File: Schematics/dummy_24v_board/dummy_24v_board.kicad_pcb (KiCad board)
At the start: 2 copper layers, 69.5 x 60 mm, 1 part, among them J1 Stack Male Edge Connector

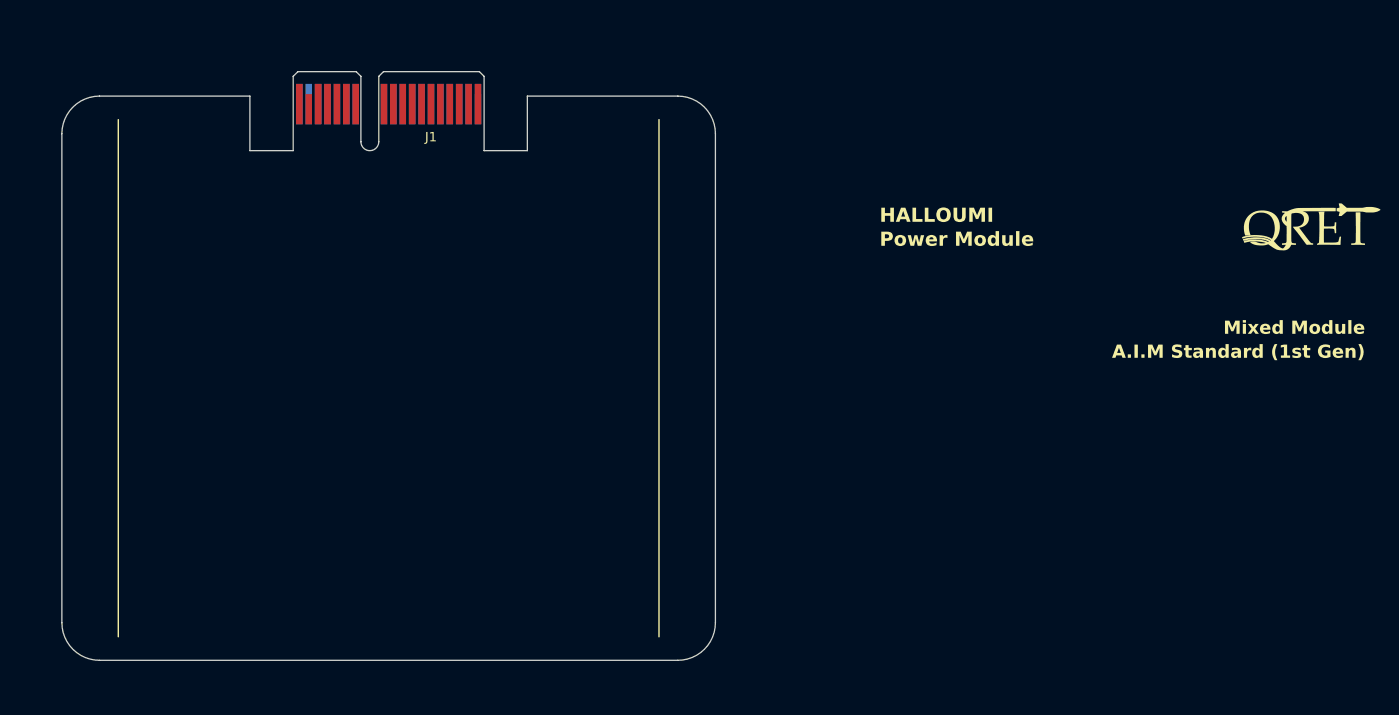
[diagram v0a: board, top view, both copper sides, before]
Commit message: added 3.3V,5V,CAN
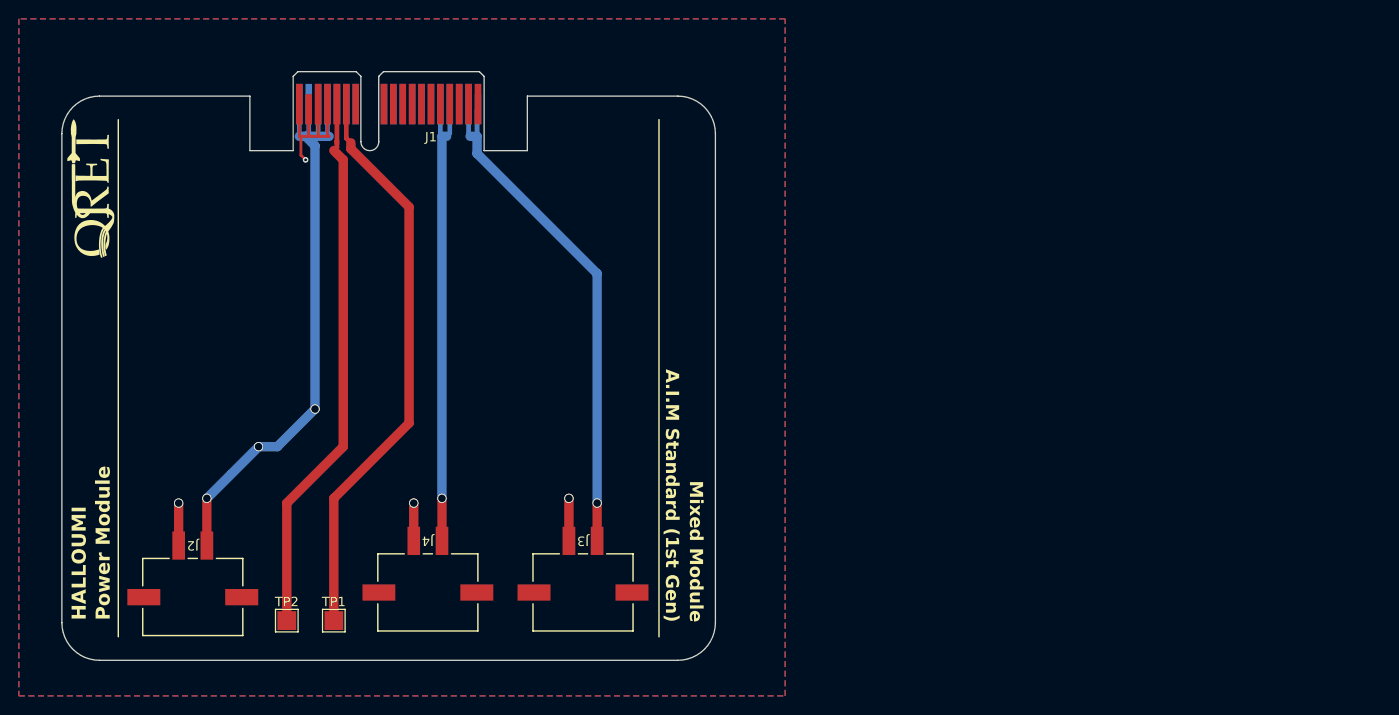
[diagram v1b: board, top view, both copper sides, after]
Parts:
- added J2: Conn_01x02_Socket, footprints:CONN_2-1445057-2_TYCO, F.Cu at (38.0, 69.5)
- added J3: Conn_01x02_Socket, footprints:CONN_2-1445057-2_TYCO, F.Cu at (79.5, 69.0)
- added J4: Conn_01x02_Socket, footprints:CONN_2-1445057-2_TYCO, F.Cu at (63.0, 69.0)
- added TP1: TestPoint, TestPoint:TestPoint_Pad_2.0x2.0mm, F.Cu at (51.5, 77.5)
- added TP2: TestPoint, TestPoint:TestPoint_Pad_2.0x2.0mm, F.Cu at (46.5, 77.5)
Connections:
- net 5.0V_A renamed +5V
- net Net-(J1-24V_C-PadA15) renamed +24V
- net Net-(J1-3.3V_A-PadA1) renamed +3.3V
- net Net-(J1-GND_C-PadB15) renamed GND
- J1 pad B13: unconnected-(J1-CAN_L-PadB13) -> CAN_L
- J1 pad B14: unconnected-(J1-CAN_H-PadB14) -> CAN_H
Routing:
- net +24V: track 0.00 -> 66.8 mm, vias 0 -> 3
- net CAN_L: track 0.00 -> 61.0 mm
- net CAN_H: track 0.00 -> 58.3 mm
- net +3.3V: track 0.00 -> 55.4 mm, vias 0 -> 1
- net +5V: track 0.00 -> 50.6 mm, vias 0 -> 1
- net GND: track 0.00 -> 32.3 mm, vias 0 -> 4
- added copper zone on B.Cu, net GND
- added copper zone on F.Cu, net GND

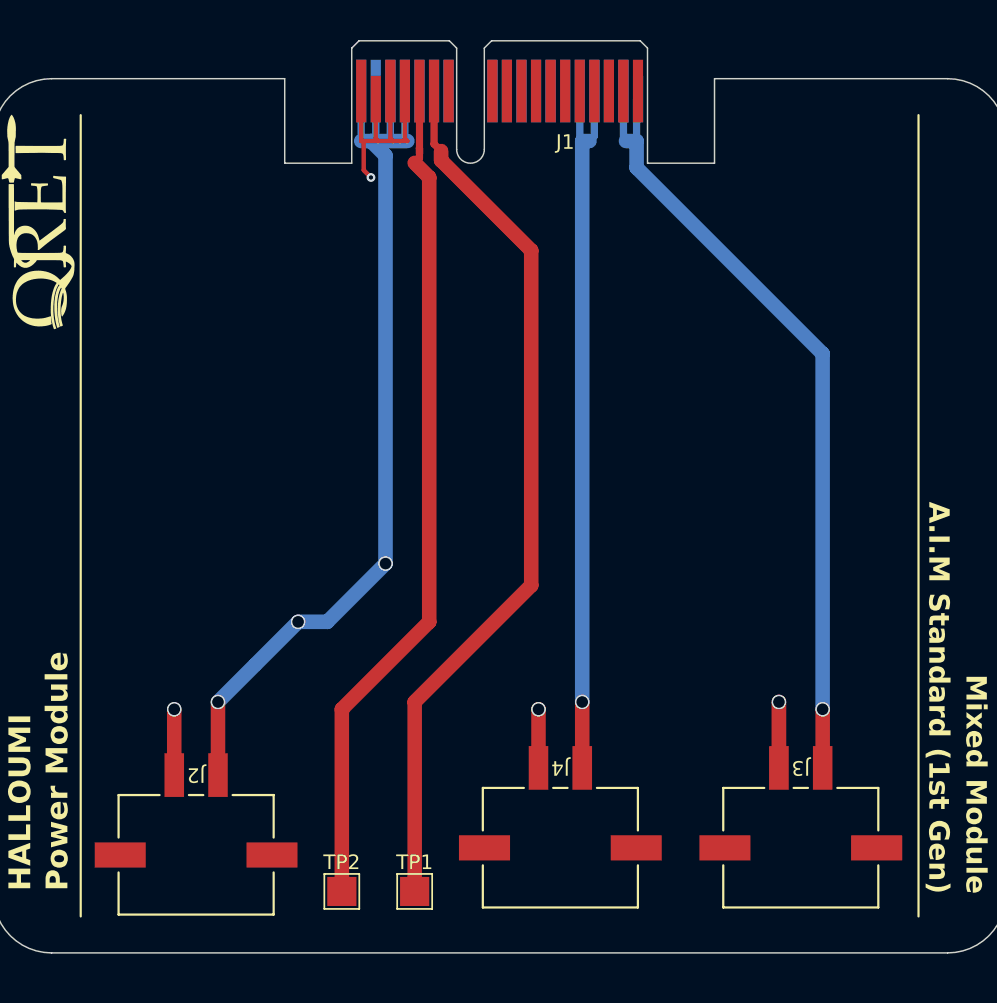
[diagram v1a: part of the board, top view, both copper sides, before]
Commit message: added two TestPoints for BATT 1&2
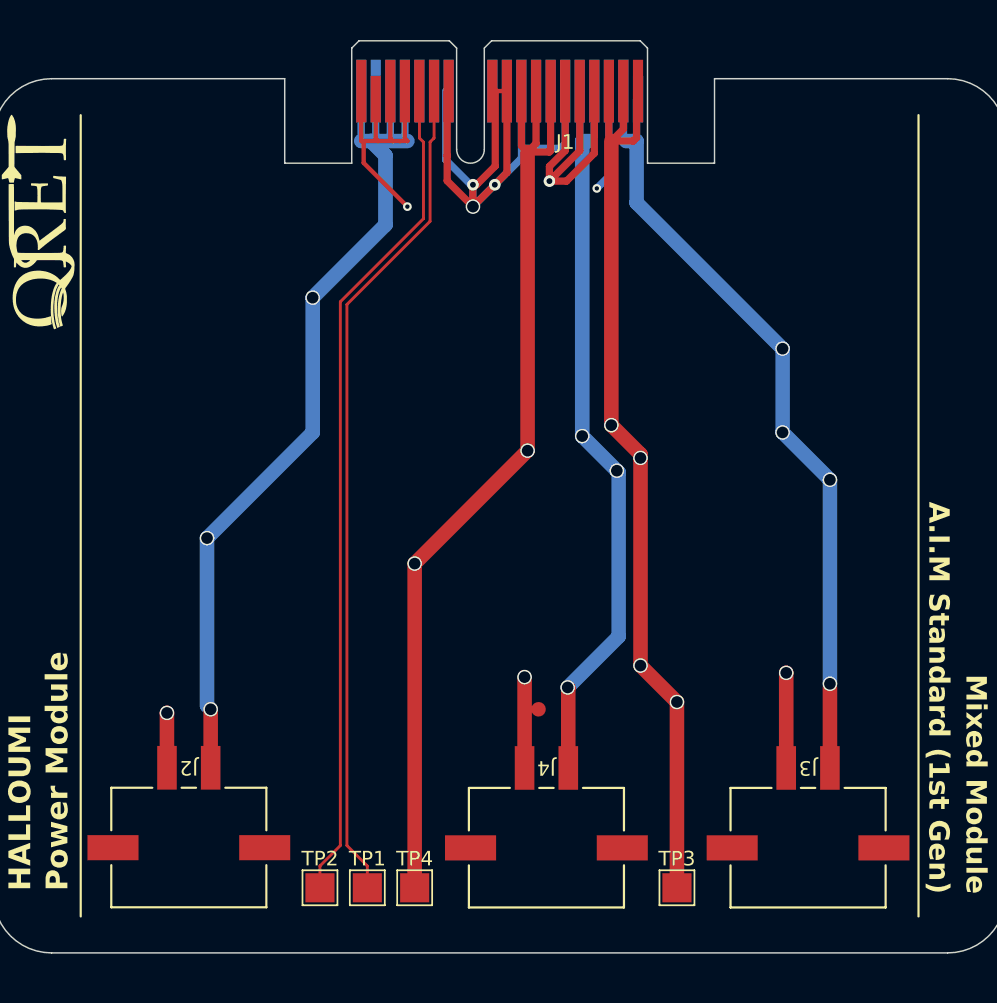
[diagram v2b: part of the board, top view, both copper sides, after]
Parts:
- added TP3: TestPoint, TestPoint:TestPoint_Pad_2.0x2.0mm, F.Cu at (69.5, 77.2)
- added TP4: TestPoint, TestPoint:TestPoint_Pad_2.0x2.0mm, F.Cu at (51.5, 77.2)
- moved TP1 3.26 mm to (48.2, 77.2)
- moved TP2 1.52 mm to (45.0, 77.2)
- moved J4 0.96 mm to (62.0, 69.0)
- moved J2 0.71 mm to (37.5, 69.0)
- moved J3 0.50 mm to (80.0, 69.0)
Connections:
- net CAN_H renamed CAN_+
- net CAN_L renamed CAN_-
- net Net-(J1-BATT_A-PadB1) renamed /BATT_1
- net Net-(J1-BATT_B-PadB7) renamed /BATT_2
- J1 pad A12: Net-(J1-GND_B-PadA12) -> GND
- J1 pad A3: Net-(J1-GND_A-PadA3) -> GND
- J1 pad A6: Net-(J1-GND_A-PadA3) -> GND
- J1 pad A7: Net-(J1-3.3V_B-PadA7) -> +3.3V
- J1 pad A8: Net-(J1-3.3V_B-PadA7) -> +3.3V
- J1 pad A9: Net-(J1-GND_B-PadA12) -> GND
- J1 pad B10: Net-(J1-GND_B-PadA12) -> GND
- J1 pad B11: Net-(J1-GND_B-PadA12) -> GND
- J1 pad B12: Net-(J1-GND_B-PadA12) -> GND
- J1 pad B4: Net-(J1-GND_A-PadA3) -> GND
- J1 pad B5: Net-(J1-GND_A-PadA3) -> GND
- J1 pad B6: Net-(J1-GND_A-PadA3) -> GND
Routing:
- net GND: track 32.3 -> 119.9 mm, vias 4 -> 9
- net /BATT_2: track 0.00 -> 68.2 mm, vias 0 -> 2
- net /BATT_1: track 0.00 -> 65.4 mm, vias 0 -> 4
- net CAN_-: track 61.0 -> 57.7 mm
- net +5V: track 50.6 -> 53.1 mm, vias 1 -> 3
- net +24V: track 66.8 -> 65.7 mm
- net CAN_+: track 58.3 -> 57.7 mm
- net +3.3V: track 55.4 -> 55.1 mm, vias 1 -> 4

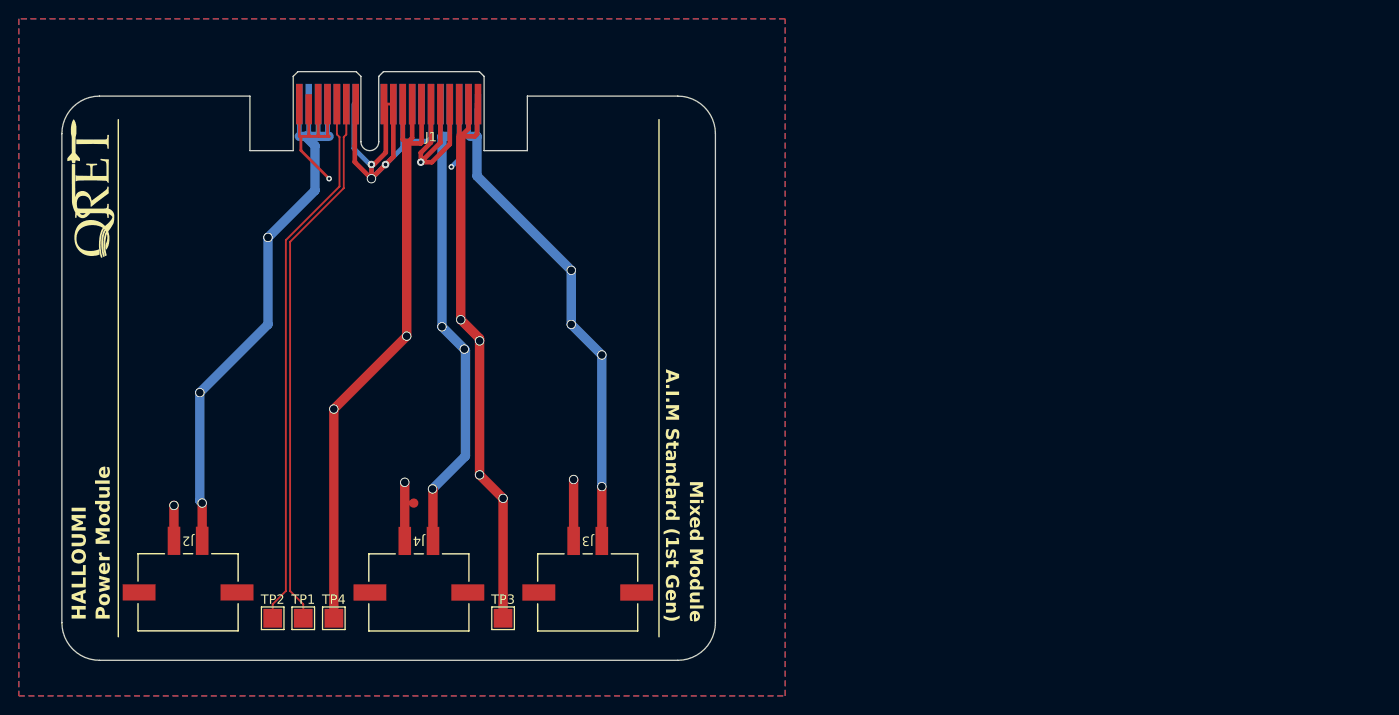
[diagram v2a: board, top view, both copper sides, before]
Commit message: gnd vias added
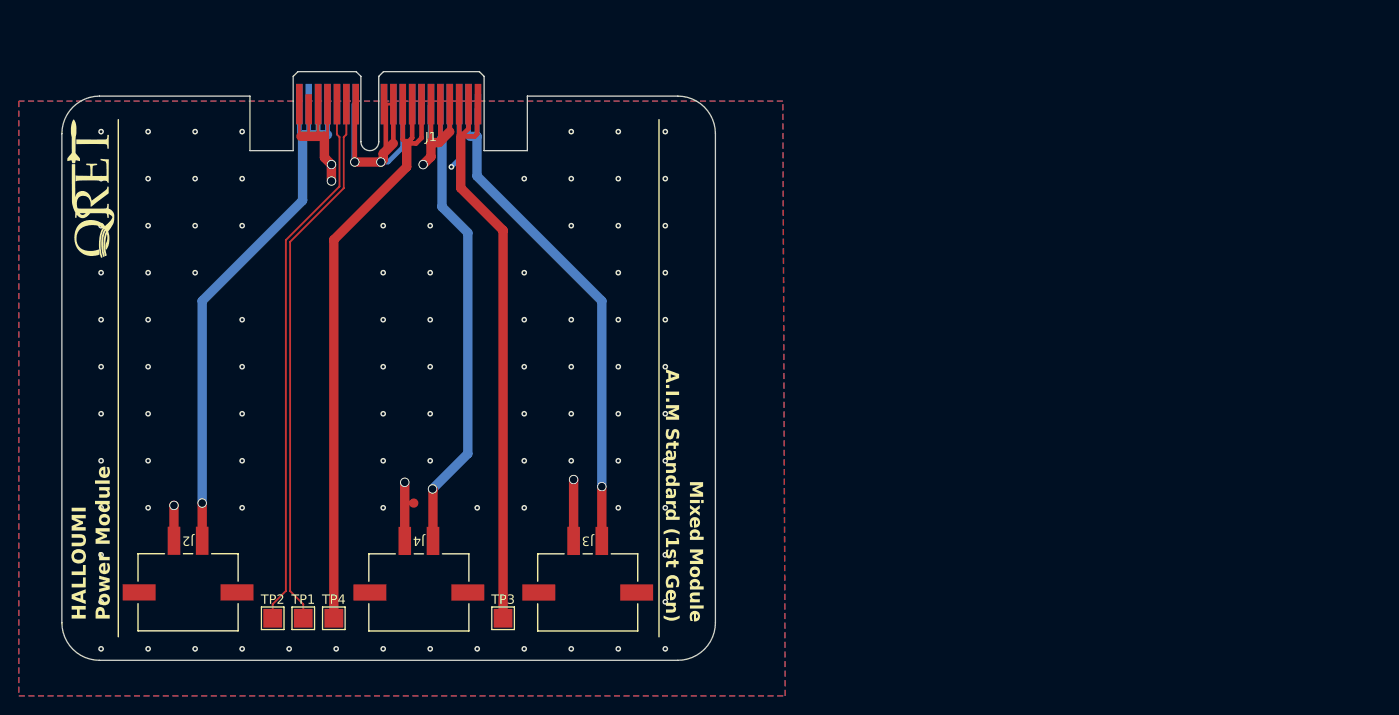
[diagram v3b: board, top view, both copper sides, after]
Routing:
- net GND: track 119.9 -> 104.0 mm, vias 9 -> 102
- net +24V: track 65.7 -> 63.4 mm, vias 3 -> 1
- net /BATT_2: track 68.2 -> 67.9 mm, vias 2 -> 0
- net +5V: track 53.1 -> 53.2 mm, vias 3 -> 1
- net /BATT_1: vias 4 -> 0
- net +3.3V: vias 4 -> 1
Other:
- board text removed: "USE GRID THAT IS SOME MULTIPLE OF 0.1mm (0.1mm, 0.2mm, 0.5mm, 1.0mm, etc)"

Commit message: Vias modified
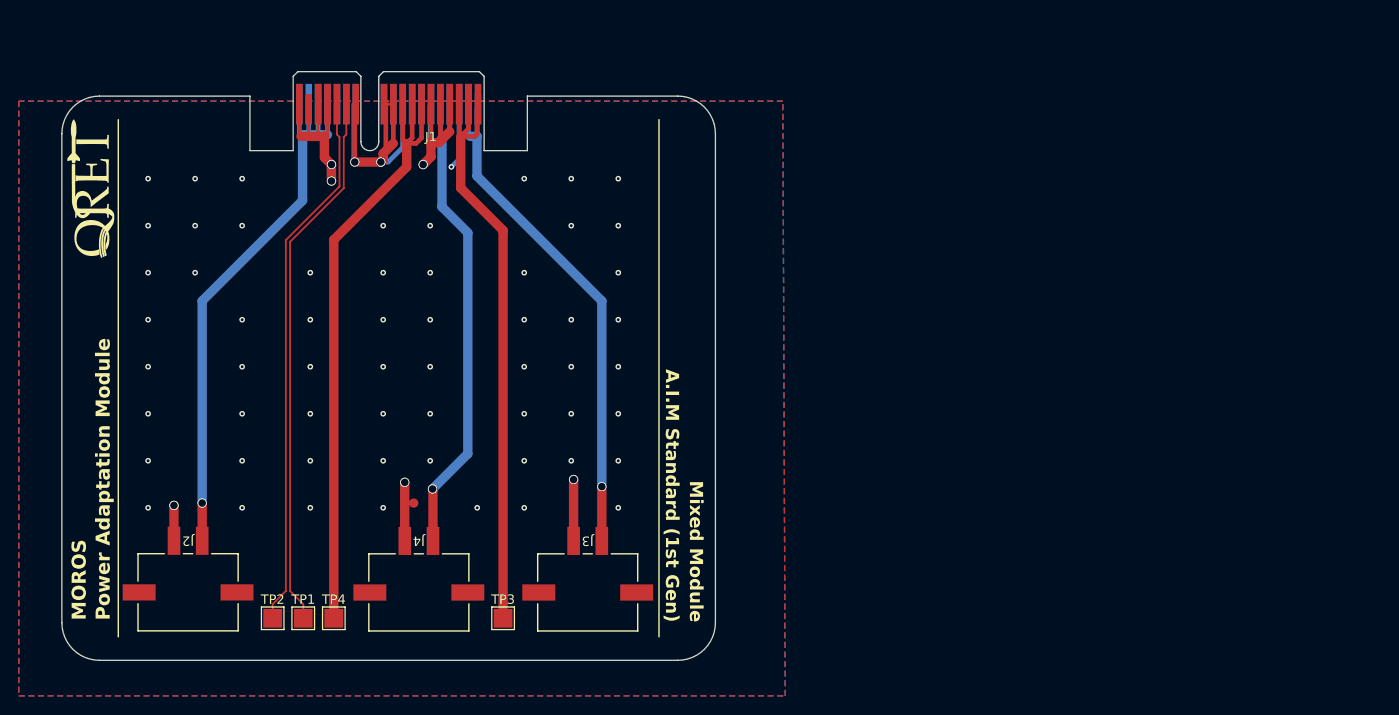
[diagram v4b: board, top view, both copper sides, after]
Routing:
- net GND: vias 102 -> 68
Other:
- board text added: "MOROS"
- board text added: "Moros V1.0 QRET Feb 2026 Johann Samuel Nana"
- board text added: "Power Adaptation Module"
- board text removed: "HALLOUMI"
- board text removed: "Power Module"

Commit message: Connectors model added
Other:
- board text added: "A.I.M Standard (2nd Gen)"
- board text added: "MORROS"
- board text added: "Morros V1.0 QRET Feb 2026 Johann Samuel Nana"
- board text removed: "A.I.M Standard (1st Gen)"
- board text removed: "MOROS"
- board text removed: "Mixed Module"
- board text removed: "Moros V1.0 QRET Feb 2026 Johann Samuel Nana"
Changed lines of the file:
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@@
 		)
 		(property "Value" "Conn_01x02_Socket"
-			(at 1.5 0 180)
+			(at 1.5 0 0)
 			(unlocked yes)
 			(layer "F.Fab")
@@
 		)
 		(property "Value" "Conn_01x02_Socket"
-			(at 1.5 0 180)
+			(at 1.5 0 0)
 			(unlocked yes)
 			(layer "F.Fab")
@@
 		)
 		(property "Value" "Conn_01x02_Socket"
-			(at 1.5 0 180)
+			(at 1.5 0 0)
 			(unlocked yes)
 			(layer "F.Fab")
@@
 		(layer "Edge.Cuts")
 	)
-	(gr_text "Moros V1.0\nQRET Feb 2026\n\nJohann Samuel Nana"
+	(gr_text "Morros V1.0\nQRET Feb 2026\n\nJohann Samuel Nana"
 		(at 56.5 44.25 0)
 		(layer "B.SilkS")
@@
 		)
 	)
-	(gr_text "A.I.M Standard (1st Gen)"
-		(at 86.649998 77.68 -90)
+	(gr_text "A.I.M Standard (2nd Gen)"
+		(at 86.649998 77.68 270)
 		(layer "F.SilkS")
 		(effects
@@
 		)
 	)
-	(gr_text "MOROS"
+	(gr_text "MORROS"
 		(at 25.3 77.47 90)
 		(layer "F.SilkS" knockout)
@@
 		)
 	)
-	(gr_text "Mixed Module"
-		(at 89.199998 77.68 -90)
-		(layer "F.SilkS")
-		(effects
-			(font
-				(size 1.4 1.4)
-				(thickness 0.25)
-				(bold yes)
-			)
-			(justify right bottom)
-		)
-	)
